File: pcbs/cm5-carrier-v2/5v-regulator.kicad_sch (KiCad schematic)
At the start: 48 parts, among them Q401 DMN21D2UFB-7B, Q402 DMN21D2UFB-7B, Q403 DMN21D2UFB-7B, U401 AZV3001FZ4-7, U402 TPS259470ARPW, U403 MAX20008AFOC/VY+T

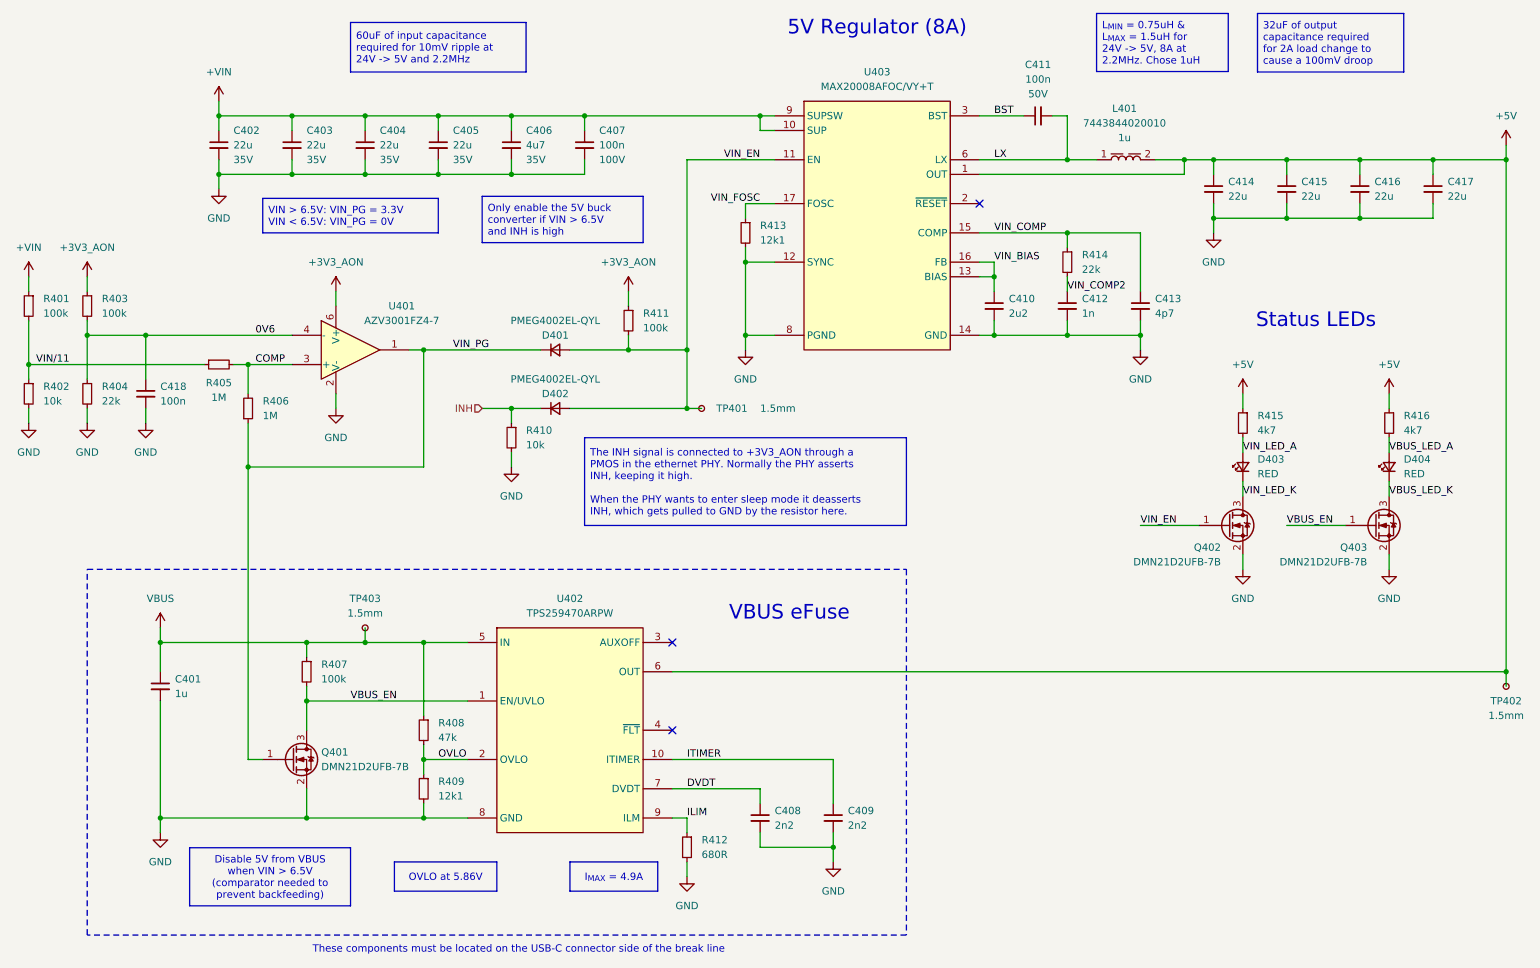
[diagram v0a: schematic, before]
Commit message: Changed UART connector to I2C
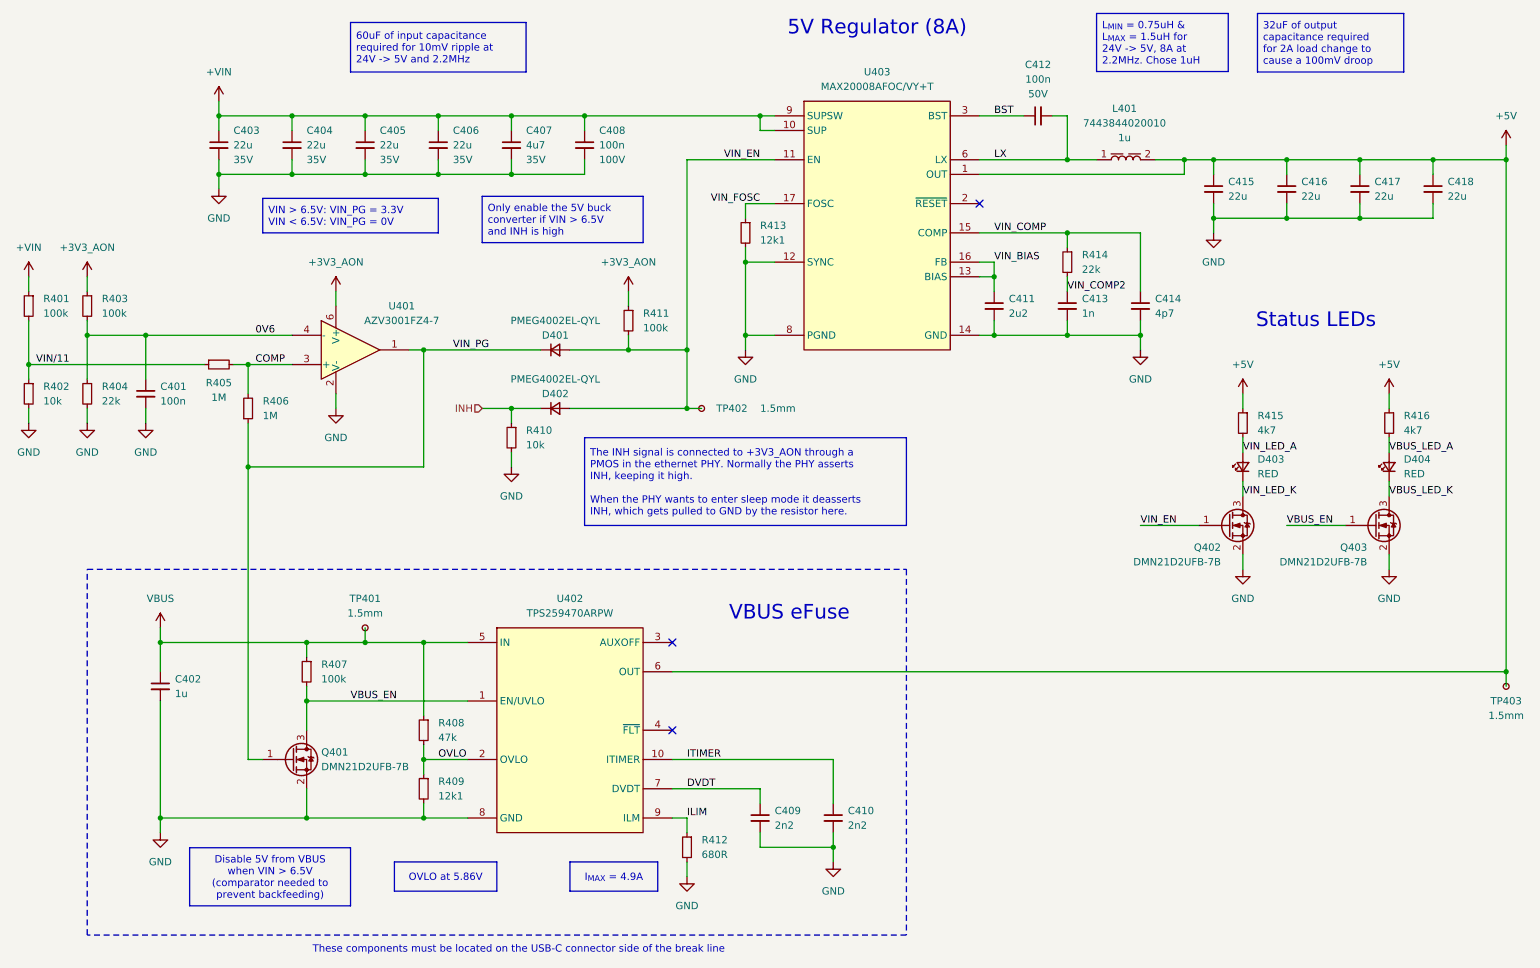
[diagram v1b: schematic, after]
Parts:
- renumbered C418 to C401, C401 to C402, C402 to C403, C403 to C404, C404 to C405, C405 to C406, C406 to C407, C407 to C408, C408 to C409, C409 to C410, C410 to C411, C411 to C412, C412 to C413, C413 to C414, C414 to C415, C415 to C416, C416 to C417, C417 to C418, TP403 to TP401, TP401 to TP402, TP402 to TP403
